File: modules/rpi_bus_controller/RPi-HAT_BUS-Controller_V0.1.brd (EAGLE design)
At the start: 65 x 56 mm, 52 parts, among them IC1 MC34063AD, IC2 ADUM1201ARZ, IC3 P89LPC922FDH,512FDH, IC4 24LC-I/OT, Q1 ASF1, T1 BC856, T2 BCP52, T3 BC847

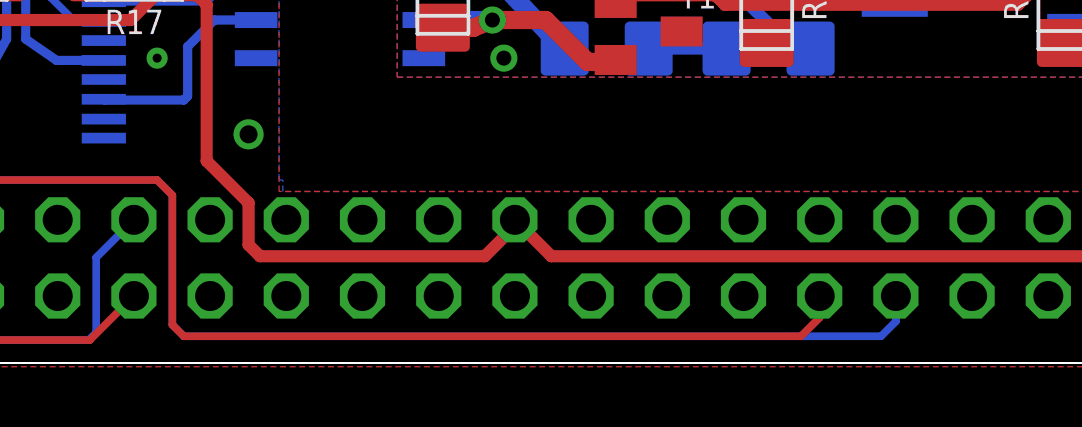
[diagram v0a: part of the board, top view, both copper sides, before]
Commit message: TXD RXD getauscht
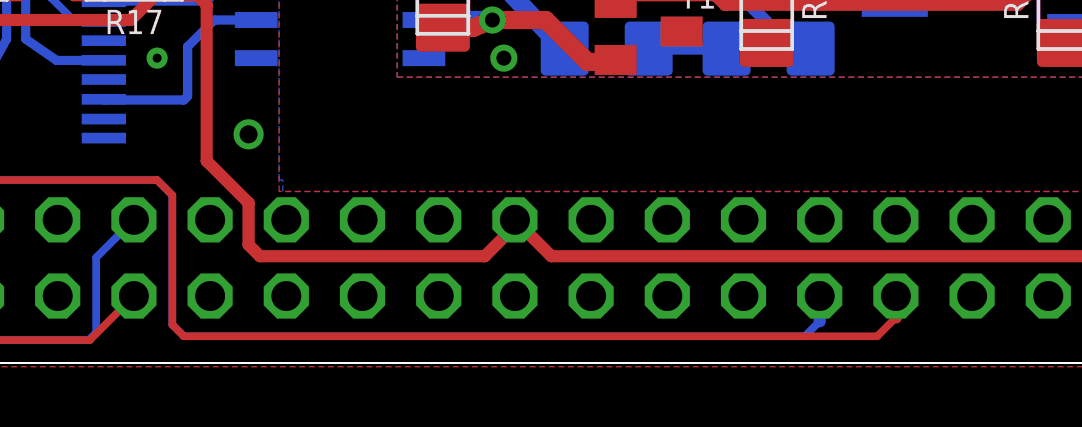
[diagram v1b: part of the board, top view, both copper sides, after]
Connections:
- net RXD: now also JP2.8; no longer JP2.10
- net TXD: now also JP2.10; no longer JP2.8
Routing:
- net TXD: track 59.9 -> 57.3 mm
- net RXD: track 48.8 -> 51.4 mm
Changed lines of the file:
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@@
 <?xml version="1.0" encoding="utf-8"?>
 <!DOCTYPE eagle SYSTEM "eagle.dtd">
-<eagle version="7.2.0">
+<eagle version="7.4.0">
 <drawing>
 <settings>
@@
 </signal>
 <signal name="TXD">
-<contactref element="JP2" pad="8"/>
 <contactref element="JP1" pad="4"/>
 <contactref element="IC3" pad="12"/>
@@
 <wire x1="15.24" y1="11.43" x2="13.97" y2="12.7" width="0.254" layer="16"/>
 <wire x1="13.97" y1="12.7" x2="12.7" y2="12.7" width="0.254" layer="16"/>
-<wire x1="49.01" y1="2.23" x2="49.01" y2="1.385" width="0.254" layer="16"/>
-<wire x1="49.01" y1="1.385" x2="48.514" y2="0.889" width="0.254" layer="16"/>
-<wire x1="48.514" y1="0.889" x2="25.273" y2="0.889" width="0.254" layer="16"/>
+<wire x1="46.47" y1="1.385" x2="45.974" y2="0.889" width="0.254" layer="16"/>
+<wire x1="45.974" y1="0.889" x2="25.273" y2="0.889" width="0.254" layer="16"/>
 <wire x1="25.273" y1="0.889" x2="24.892" y2="1.27" width="0.254" layer="16"/>
 <wire x1="24.892" y1="1.27" x2="24.892" y2="5.588" width="0.254" layer="16"/>
@@
 <wire x1="10.668" y1="11.938" x2="11.43" y2="12.7" width="0.254" layer="16"/>
 <wire x1="11.43" y1="12.7" x2="12.7" y2="12.7" width="0.254" layer="16"/>
+<contactref element="JP2" pad="10"/>
+<wire x1="46.47" y1="2.23" x2="46.47" y2="1.385" width="0.4064" layer="16"/>
 </signal>
 <signal name="RXD">
-<contactref element="JP2" pad="10"/>
 <contactref element="JP1" pad="5"/>
 <contactref element="IC3" pad="11"/>
@@
 <wire x1="14.732" y1="9.398" x2="13.97" y2="10.16" width="0.254" layer="16"/>
 <wire x1="13.97" y1="10.16" x2="12.7" y2="10.16" width="0.254" layer="16"/>
-<wire x1="46.47" y1="2.23" x2="46.47" y2="1.512" width="0.254" layer="1"/>
-<wire x1="46.47" y1="1.512" x2="45.847" y2="0.889" width="0.254" layer="1"/>
-<wire x1="45.847" y1="0.889" x2="25.273" y2="0.889" width="0.254" layer="1"/>
+<wire x1="49.01" y1="1.512" x2="48.387" y2="0.889" width="0.254" layer="1"/>
+<wire x1="48.387" y1="0.889" x2="25.273" y2="0.889" width="0.254" layer="1"/>
 <wire x1="25.273" y1="0.889" x2="24.892" y2="1.27" width="0.254" layer="1"/>
 <wire x1="24.892" y1="1.27" x2="24.892" y2="5.588" width="0.254" layer="1"/>
@@
 <wire x1="14.732" y1="9.398" x2="13.97" y2="10.16" width="0.254" layer="1"/>
 <wire x1="13.97" y1="10.16" x2="12.7" y2="10.16" width="0.254" layer="1"/>
+<contactref element="JP2" pad="8"/>
+<wire x1="49.01" y1="1.512" x2="49.01" y2="2.23" width="0.4064" layer="1"/>
 </signal>
 <signal name="ID_SC">
